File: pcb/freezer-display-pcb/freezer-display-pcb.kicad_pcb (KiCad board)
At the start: 2 copper layers, 41.6 x 60.3 mm, 3 parts, among them J2 IT8951 board connector castel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, SW1 SW_Push, U1 ProS3

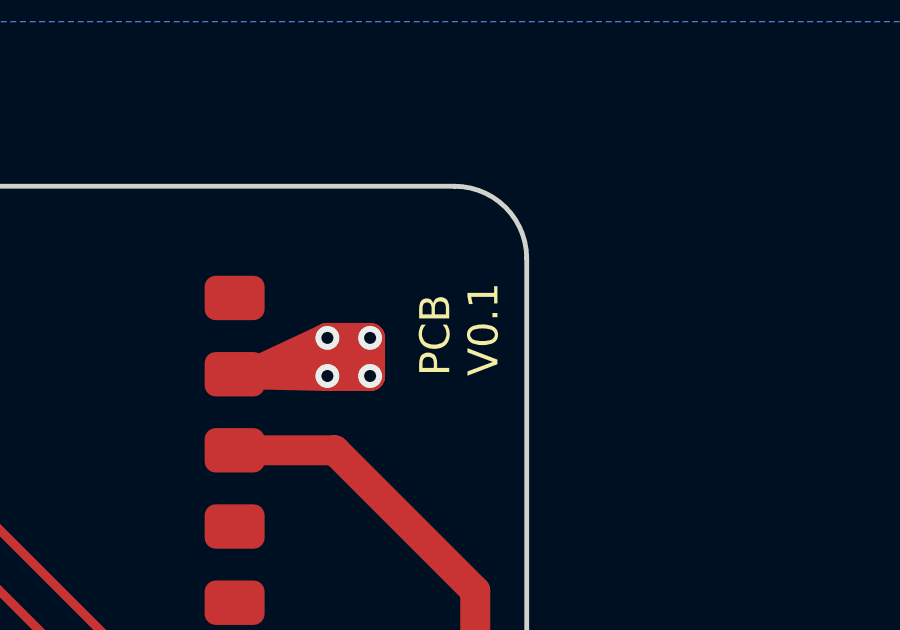
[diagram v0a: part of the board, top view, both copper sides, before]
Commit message: Fixed swapped net labels
MISO and MOSI nets were swapped, but the functionality of the PCB was correct. Now updated to avoid confusion. PCB design has been assembled and seems to work.  Added basic documentation for the PCB.
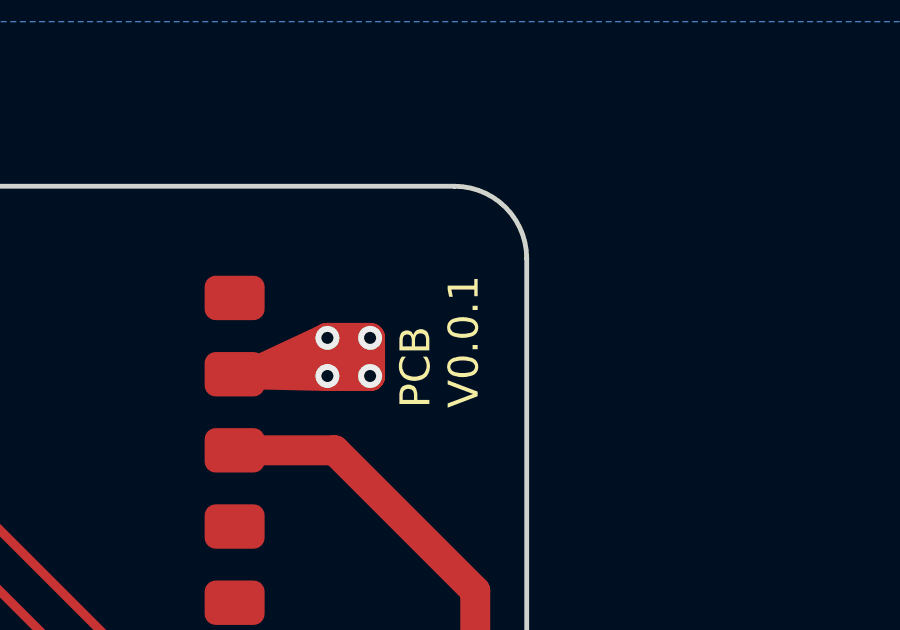
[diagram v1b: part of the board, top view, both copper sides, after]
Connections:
- J2 pad 3: MOSI -> MISO
- J2 pad 4: MISO -> MOSI
- U1 pad 33: MOSI -> MISO
- U1 pad 34: MISO -> MOSI
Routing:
- net MOSI: track 68.1 -> 69.9 mm, vias 0 -> 1
- net MISO: track 69.9 -> 68.1 mm, vias 1 -> 0
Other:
- board text added: "PCB V0.0.1"
- board text removed: "PCB V0.1"
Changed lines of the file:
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@@
 			(layers "*.Cu" "*.Mask")
 			(remove_unused_layers no)
-			(net 11 "MOSI")
+			(net 18 "MISO")
 			(pinfunction "Pin_3")
 			(pintype "passive")
@@
 			(layers "*.Cu" "*.Mask")
 			(remove_unused_layers no)
-			(net 18 "MISO")
+			(net 11 "MOSI")
 			(pinfunction "Pin_4")
 			(pintype "passive")
@@
 			(layers "F.Cu" "F.Paste" "F.Mask")
 			(roundrect_rratio 0.25)
-			(net 11 "MOSI")
+			(net 18 "MISO")
 			(pinfunction "IO37")
 			(pintype "bidirectional")
@@
 			(layers "F.Cu" "F.Paste" "F.Mask")
 			(roundrect_rratio 0.25)
-			(net 18 "MISO")
+			(net 11 "MOSI")
 			(pinfunction "IO35")
 			(pintype "bidirectional")
@@
 		(layer "Edge.Cuts")
 	)
-	(gr_text "PCB\nV0.1"
-		(at 185.2676 41.91 90)
+	(gr_text "PCB\nV0.0.1"
+		(at 184.6072 42.9768 90)
 		(layer "F.SilkS")
 		(effects
@@
 	)
 	(segment
-		(start 186.6016 94.552)
-		(end 186.6016 95.8596)
-		(width 0.3)
-		(layer "F.Cu")
-		(net 11)
-	)
-	(segment
-		(start 173.1772 53.6956)
-		(end 173.1772 81.1276)
-		(width 0.3)
-		(layer "F.Cu")
-		(net 11)
-	)
-	(segment
-		(start 161.3408 41.8592)
-		(end 173.1772 53.6956)
-		(width 0.3)
-		(layer "F.Cu")
-		(net 11)
-	)
-	(segment
-		(start 173.1772 81.1276)
-		(end 186.6016 94.552)
-		(width 0.3)
-		(layer "F.Cu")
-		(net 11)
-	)
-	(segment
-		(start 157.6832 41.8592)
-		(end 161.3408 41.8592)
-		(width 0.3)
-		(layer "F.Cu")
-		(net 11)
-	)
-	(segment
 		(start 183.7944 90.3732)
 		(end 174.046597 80.625397)
 		(width 0.3)
 		(layer "F.Cu")
-		(net 18)
+		(net 11)
 	)
 	(segment
@@
 		(width 0.3)
 		(layer "F.Cu")
-		(net 18)
+		(net 11)
 	)
 	(segment
@@
 		(width 0.3)
 		(layer "F.Cu")
-		(net 18)
+		(net 11)
 	)
 	(segment
@@
 		(width 0.3)
 		(layer "F.Cu")
-		(net 18)
+		(net 11)
 	)
 	(segment
@@
 		(width 0.3)
 		(layer "F.Cu")
-		(net 18)
+		(net 11)
 	)
 	(via
@@
 		(drill 0.3)
 		(layers "F.Cu" "B.Cu")
-		(net 18)
+		(net 11)
 	)
 	(segment
@@
 		(width 0.3)
 		(layer "B.Cu")
-		(net 18)
+		(net 11)
 	)
 	(segment
@@
 		(width 0.3)
 		(layer "B.Cu")
+		(net 11)
+	)
+	(segment
+		(start 186.6016 94.552)
+		(end 186.6016 95.8596)
+		(width 0.3)
+		(layer "F.Cu")
 		(net 18)
 	)
+	(segment
+		(start 173.1772 53.6956)
+		(end 173.1772 81.1276)
+		(width 0.3)
+		(layer "F.Cu")
+		(net 18)
+	)
+	(segment
+		(start 161.3408 41.8592)
+		(end 173.1772 53.6956)
+		(width 0.3)
+		(layer "F.Cu")
+		(net 18)
+	)
+	(segment
+		(start 173.1772 81.1276)
+		(end 186.6016 94.552)
+		(width 0.3)
+		(layer "F.Cu")
+		(net 18)
+	)
+	(segment
+		(start 157.6832 41.8592)
+		(end 161.3408 41.8592)
+		(width 0.3)
+		(layer "F.Cu")
+		(net 18)
+	)
